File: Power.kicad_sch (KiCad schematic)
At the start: 51 parts, among them U1 STPMIC1APQR

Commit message: Layout started
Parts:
- added D1, D10, D11, D12, D13, D14, D2, D3, D4, D5, D6, D7, D8, D9: Red, SparkFun-LED:LED_0603_1608Metric, symbol SparkFun-LED:LED_Red_0603
- added R1, R10, R11, R14, R15, R16, R2, R3, R4, R5, R6, R7, R8, R9: 680, Resistor_SMD:R_0402_1005Metric, symbol SparkFun-Resistor:R
- renumbered R1 to R12, R2 to R13
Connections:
- net BSTOUT: now also D12.2 (A)
- net GND: now also R1.2, R10.2, R11.2, R14.2, R15.2, R16.2, R2.2, R3.2, R4.2, R5.2, R6.2, R7.2, R8.2, R9.2
- net LDO5OUT: now also D10.2 (A)
- net LDO6OUT: now also D11.2 (A)
- net VBUS_HOST: now also D14.2 (A)
- net VBUS_OTG: now also D13.2 (A)
- net VDD: now also D4.2 (A)
- net VDDA: now also D6.2 (A)
- net VDD_AUX: now also D5.2 (A)
- net VDD_CORE: now also D2.2 (A)
- net VDD_DDR: now also D3.2 (A)
- net VDD_NAND: now also D7.2 (A)
- net VDD_USB: now also D9.2 (A)
- net VIN: now also D1.2 (A)
- net VTT_DDR: now also D8.2 (A)
- new net: D8.1 (K), R8.1
- new net: D6.1 (K), R6.1
- new net: D2.1 (K), R2.1
- new net: D14.1 (K), R16.1
- new net: D3.1 (K), R3.1
- new net: D11.1 (K), R11.1
- new net: D10.1 (K), R10.1
- new net: D4.1 (K), R4.1
- new net: D7.1 (K), R7.1
- new net: D12.1 (K), R14.1
- new net: D5.1 (K), R5.1
- new net: D9.1 (K), R9.1
- new net: D1.1 (K), R1.1
- new net: D13.1 (K), R15.1
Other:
- moved on the sheet: CBUCK1IN1, CBUCK2IN1, CBUCK3IN1, CBUCK4IN1, CLDO16IN1, CLDO25IN1, CLDO3IN1, CVIN1, CVLXBST1, LXB1, NT1, NT2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

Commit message: Component placement
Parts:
- added H1, H2, H3, H4: MountingHole, MountingHole:MountingHole_3.2mm_M3, symbol Mechanical:MountingHole
- added TP22, TP23: RCWCTE, footprints:TP420X150, symbol RCWCTE:RCWCTE
- R12: footprint SparkFun-Resistor:R_0603_1608Metric -> Resistor_SMD:R_0402_1005Metric
- R13: footprint SparkFun-Resistor:R_0603_1608Metric -> LED_SMD:LED_0402_1005Metric
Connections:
- net GND: now also TP23.1
- net VIN: now also TP22.1

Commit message: Routed PMIC and started on MPU
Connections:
- net SWIN is gone; now on net BSTOUT: NT1.2, U1.37 (SWIN)
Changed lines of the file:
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@@
+	)
+	(junction
+		(at 250.19 83.82)
+		(diameter 0)
+		(color 0 0 0 0)
 	)
 	(junction
@@
 	(junction
 		(at 167.64 116.84)
+		(diameter 0)
+		(color 0 0 0 0)
+	)
+	(junction
+		(at 260.35 83.82)
 		(diameter 0)
 		(color 0 0 0 0)
@@
 	(wire
 		(pts
+			(xy 250.19 77.47) (xy 260.35 77.47)
+		)
+		(stroke
+			(width 0)
+			(type default)
+		)
+	)
+	(wire
+		(pts
 			(xy 22.86 44.45) (xy 35.56 44.45)
 		)
@@
 	(wire
 		(pts
+			(xy 260.35 77.47) (xy 260.35 83.82)
+		)
+		(stroke
+			(width 0)
+			(type default)
+		)
+	)
+	(wire
+		(pts
 			(xy 256.54 25.4) (xy 265.43 25.4)
 		)
@@
 	(wire
 		(pts
+			(xy 250.19 83.82) (xy 250.19 77.47)
+		)
+		(stroke
+			(width 0)
+			(type default)
+		)
+	)
+	(wire
+		(pts
 			(xy 193.04 120.65) (xy 193.04 116.84)
 		)
@@
 	(wire
 		(pts
-			(xy 257.81 83.82) (xy 267.97 83.82)
+			(xy 257.81 83.82) (xy 260.35 83.82)
 		)
 		(stroke
@@
 	(wire
 		(pts
-			(xy 242.57 83.82) (xy 252.73 83.82)
+			(xy 242.57 83.82) (xy 250.19 83.82)
 		)
 		(stroke
@@
 	(wire
 		(pts
+			(xy 250.19 83.82) (xy 252.73 83.82)
+		)
+		(stroke
+			(width 0)
+			(type default)
+		)
+	)
+	(wire
+		(pts
 			(xy 115.57 110.49) (xy 115.57 115.57)
 		)
@@
 		)
 		(stroke
+			(width 0)
+			(type default)
+		)
+	)
+	(wire
+		(pts
+			(xy 260.35 83.82) (xy 267.97 83.82)
+		)
+		(stroke

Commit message: Routing DDR
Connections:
- net VIN: no longer CLDO3IN1.1, NT3.2, U1.13 (LDO3IN)
- new net LDO3IN: CLDO3IN1.1, NT3.2, U1.13 (LDO3IN)
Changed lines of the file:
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@@
 	)
 	(junction
-		(at 256.54 25.4)
-		(diameter 0)
-		(color 0 0 0 0)
-	)
-	(junction
 		(at 104.14 181.61)
 		(diameter 0)
@@
 	(wire
 		(pts
-			(xy 256.54 22.86) (xy 256.54 25.4)
-		)
-		(stroke
-			(width 0)
-			(type default)
-		)
-	)
-	(wire
-		(pts
 			(xy 167.64 143.51) (xy 179.07 143.51)
 		)
@@
 					(unit 1)
 				)
-			)
-		)
-	)
-	(symbol
-		(lib_id "SparkFun-PowerSymbol:VIN")
-		(at 256.54 22.86 0)
-		(unit 1)
-		(exclude_from_sim no)
-		(in_bom yes)
-		(on_board yes)
-		(dnp no)
-		(fields_autoplaced yes)
-		(property "Reference" "#PWR08"
-			(at 256.54 26.67 0)
-			(effects
-				(font
-					(size 1.27 1.27)
-				)
-				(hide yes)
-			)
-		)
-		(property "Value" "VIN"
-			(at 256.54 19.05 0)
-			(do_not_autoplace yes)
-			(effects
-				(font
-					(size 1.27 1.27)
-				)
-			)
-		)
-		(property "Footprint" ""
-			(at 256.54 22.86 0)
-			(effects
-				(font
-					(size 1.27 1.27)
-				)
-				(hide yes)
-			)
-		)
-		(property "Datasheet" ""
-			(at 256.54 22.86 0)
-			(effects
-				(font
-					(size 1.27 1.27)
-				)
-				(hide yes)
-			)
-		)
-		(property "Description" "Power symbol creates a global label with name \"VIN\""
-			(at 256.54 22.86 0)
-			(effects
-				(font
-					(size 1.27 1.27)
-				)
-				(hide yes)
-			)
-		)
-		(pin "1"
-		)
-		(instances
-			(project "SBC"
-				(path "/21bb932a-ec67-4661-9215-0551f718d1c0/62ec818c-3f4b-42f5-b6cb-504a45fcd8bf"
-					(reference "#PWR08")
-					(unit 1)
-				)

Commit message: I am not good at routing
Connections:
- net BSTOUT: no longer NT1.2, U1.37 (SWIN)
- new net SWIN: NT1.2, U1.37 (SWIN)
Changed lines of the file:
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@@
 	(generator_version "8.0")
 	(paper "A4")
+	(bus_alias "BSTOUT"
+		(members "SWIN")
+	)
 	(junction
 		(at 95.25 181.61)
@@
 	)
 	(junction
-		(at 250.19 83.82)
-		(diameter 0)
-		(color 0 0 0 0)
-	)
-	(junction
 		(at 33.02 46.99)
 		(diameter 0)
@@
 	(junction
 		(at 167.64 116.84)
-		(diameter 0)
-		(color 0 0 0 0)
-	)
-	(junction
-		(at 260.35 83.82)
 		(diameter 0)
 		(color 0 0 0 0)
@@
 	(wire
 		(pts
-			(xy 250.19 77.47) (xy 260.35 77.47)
-		)
-		(stroke
-			(width 0)
-			(type default)
-		)
-	)
-	(wire
-		(pts
 			(xy 22.86 44.45) (xy 35.56 44.45)
 		)
@@
 	(wire
 		(pts
-			(xy 260.35 77.47) (xy 260.35 83.82)
-		)
-		(stroke
-			(width 0)
-			(type default)
-		)
-	)
-	(wire
-		(pts
 			(xy 256.54 25.4) (xy 265.43 25.4)
 		)
@@
 	(wire
 		(pts
-			(xy 250.19 83.82) (xy 250.19 77.47)
-		)
-		(stroke
-			(width 0)
-			(type default)
-		)
-	)
-	(wire
-		(pts
 			(xy 193.04 120.65) (xy 193.04 116.84)
 		)
@@
 	(wire
 		(pts
-			(xy 257.81 83.82) (xy 260.35 83.82)
+			(xy 257.81 83.82) (xy 267.97 83.82)
 		)
 		(stroke
@@
 	(wire
 		(pts
-			(xy 242.57 83.82) (xy 250.19 83.82)
+			(xy 242.57 83.82) (xy 252.73 83.82)
 		)
 		(stroke
@@
 	(wire
 		(pts
-			(xy 250.19 83.82) (xy 252.73 83.82)
-		)
-		(stroke
-			(width 0)
-			(type default)
-		)
-	)
-	(wire
-		(pts
 			(xy 115.57 110.49) (xy 115.57 115.57)
 		)
@@
 		)
 		(stroke
-			(width 0)
-			(type default)
-		)
-	)
-	(wire
-		(pts
-			(xy 260.35 83.82) (xy 267.97 83.82)
-		)
-		(stroke

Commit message: Everything is placed
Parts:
- removed NT1, NT2, NT3: NetTie_2, NetTie:NetTie-2_SMD_Pad0.5mm, symbol Device:NetTie_2
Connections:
- net LDO3IN is gone; now on net VDD_DDR: CLDO3IN1.1, U1.13 (LDO3IN)
- net SWIN is gone; now on net BSTOUT: U1.37 (SWIN)
- net VIO is gone; now on net VDD: R12.1, R13.1, U1.42 (VIO)
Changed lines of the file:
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@@
 	(generator_version "8.0")
 	(paper "A4")
-	(bus_alias "BSTOUT"
-		(members "SWIN")
-	)
 	(junction
 		(at 95.25 181.61)
@@
 	(wire
 		(pts
-			(xy 257.81 101.6) (xy 267.97 101.6)
-		)
-		(stroke
-			(width 0)
-			(type default)
-		)
-	)
-	(wire
-		(pts
 			(xy 33.02 46.99) (xy 35.56 46.99)
 		)
@@
 	(wire
 		(pts
-			(xy 257.81 92.71) (xy 267.97 92.71)
-		)
-		(stroke
-			(width 0)
-			(type default)
-		)
-	)
-	(wire
-		(pts
 			(xy 157.48 181.61) (xy 157.48 184.15)
 		)
@@
 	(wire
 		(pts
-			(xy 242.57 101.6) (xy 252.73 101.6)
+			(xy 242.57 101.6) (xy 267.97 101.6)
 		)
 		(stroke
@@
 	(wire
 		(pts
-			(xy 257.81 83.82) (xy 267.97 83.82)
-		)
-		(stroke
-			(width 0)
-			(type default)
-		)
-	)
-	(wire
-		(pts
 			(xy 22.86 52.07) (xy 35.56 52.07)
 		)
@@
 	(wire
 		(pts
-			(xy 242.57 83.82) (xy 252.73 83.82)
+			(xy 242.57 83.82) (xy 267.97 83.82)
 		)
 		(stroke
@@
 	(wire
 		(pts
-			(xy 242.57 92.71) (xy 252.73 92.71)
+			(xy 242.57 92.71) (xy 267.97 92.71)
 		)
 		(stroke
@@
 	)
 	(symbol
-		(lib_id "Device:NetTie_2")
-		(at 255.27 83.82 0)
-		(unit 1)
-		(exclude_from_sim no)
-		(in_bom no)
-		(on_board yes)
-		(dnp no)
-		(fields_autoplaced yes)
-		(property "Reference" "NT1"
-			(at 255.27 78.74 0)
-			(effects
-				(font
-					(size 1.27 1.27)
-				)
-			)
-		)
-		(property "Value" "NetTie_2"
-			(at 255.27 81.28 0)
-			(effects
-				(font
-					(size 1.27 1.27)
-				)
-			)
-		)
-		(property "Footprint" "NetTie:NetTie-2_SMD_Pad0.5mm"
-			(at 255.27 83.82 0)
-			(effects
-				(font
-					(size 1.27 1.27)
-				)
-				(hide yes)
-			)
-		)
-		(property "Datasheet" "~"
-			(at 255.27 83.82 0)
-			(effects
-				(font
-					(size 1.27 1.27)
-				)
-				(hide yes)
-			)
-		)
-		(property "Description" "Net tie, 2 pins"
-			(at 255.27 83.82 0)
-			(effects
-				(font
-					(size 1.27 1.27)
-				)
-				(hide yes)
-			)
-		)
-		(pin "2"
-		)
-		(pin "1"
-		)
-		(instances
-			(project ""
-				(path "/21bb932a-ec67-4661-9215-0551f718d1c0/62ec818c-3f4b-42f5-b6cb-504a45fcd8bf"
-					(reference "NT1")
-					(unit 1)
-				)
-			)
-		)
-	)
-	(symbol
 		(lib_id "SparkFun-Resistor:R")
 		(at 138.43 80.01 90)
@@
 	)
 	(symbol
-		(lib_id "Device:NetTie_2")
-		(at 255.27 92.71 0)
-		(unit 1)
-		(exclude_from_sim no)
-		(in_bom no)
-		(on_board yes)
-		(dnp no)
-		(fields_autoplaced yes)
-		(property "Reference" "NT2"
-			(at 255.27 87.63 0)
-			(effects
-				(font
-					(size 1.27 1.27)
-				)
-			)
-		)
-		(property "Value" "NetTie_2"
-			(at 255.27 90.17 0)
-			(effects
-				(font
-					(size 1.27 1.27)
-				)
-			)
-		)
-		(property "Footprint" "NetTie:NetTie-2_SMD_Pad0.5mm"
-			(at 255.27 92.71 0)
-			(effects
-				(font
-					(size 1.27 1.27)
-				)
-				(hide yes)
-			)
-		)
-		(property "Datasheet" "~"
-			(at 255.27 92.71 0)
-			(effects
-				(font
-					(size 1.27 1.27)
-				)
-				(hide yes)
-			)
-		)
-		(property "Description" "Net tie, 2 pins"
-			(at 255.27 92.71 0)
-			(effects
-				(font
-					(size 1.27 1.27)
-				)
-				(hide yes)
-			)
-		)
-		(pin "2"
-		)
-		(pin "1"
-		)
-		(instances
-			(project "SBC"
-				(path "/21bb932a-ec67-4661-9215-0551f718d1c0/62ec818c-3f4b-42f5-b6cb-504a45fcd8bf"
-					(reference "NT2")
-					(unit 1)
-				)
-			)
-		)
-	)
-	(symbol
 		(lib_id "power:GND")
 		(at 127 48.26 0)
@@
 					(unit 1)
 				)
-			)
-		)
-	)
-	(symbol
-		(lib_id "Device:NetTie_2")
-		(at 255.27 101.6 0)
-		(unit 1)
-		(exclude_from_sim no)
-		(in_bom no)
-		(on_board yes)
-		(dnp no)
-		(fields_autoplaced yes)
-		(property "Reference" "NT3"
-			(at 255.27 96.52 0)
-			(effects
-				(font
-					(size 1.27 1.27)
-				)
-			)
-		)
-		(property "Value" "NetTie_2"
-			(at 255.27 99.06 0)
-			(effects
-				(font
-					(size 1.27 1.27)
-				)
-			)
-		)
-		(property "Footprint" "NetTie:NetTie-2_SMD_Pad0.5mm"
-			(at 255.27 101.6 0)
-			(effects
-				(font
-					(size 1.27 1.27)
-				)
-				(hide yes)
-			)
-		)
-		(property "Datasheet" "~"
-			(at 255.27 101.6 0)
-			(effects
-				(font
-					(size 1.27 1.27)
-				)
-				(hide yes)
-			)
-		)
-		(property "Description" "Net tie, 2 pins"
-			(at 255.27 101.6 0)
-			(effects
-				(font
-					(size 1.27 1.27)
-				)
-				(hide yes)
-			)
-		)
-		(pin "2"
-		)
-		(pin "1"
-		)
-		(instances
-			(project "SBC"
-				(path "/21bb932a-ec67-4661-9215-0551f718d1c0/62ec818c-3f4b-42f5-b6cb-504a45fcd8bf"
-					(reference "NT3")
-					(unit 1)
-				)

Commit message: Started an entire reroute
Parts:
- D1, D10, D11, D12, D13, D14, D2, D3, D4, D5, D6, D7, D8, D9: footprint SparkFun-LED:LED_0603_1608Metric -> LED_SMD:LED_0603_1608Metric
- TP1, TP10, TP11, TP12, TP13, TP14, TP15, TP16, TP2, TP3, TP4, TP5, TP6, TP7, TP8, TP9: footprint SparkFun-Connector:TestPoint-0.5mm -> TestPoint:TestPoint_Pad_1.0x1.0mm

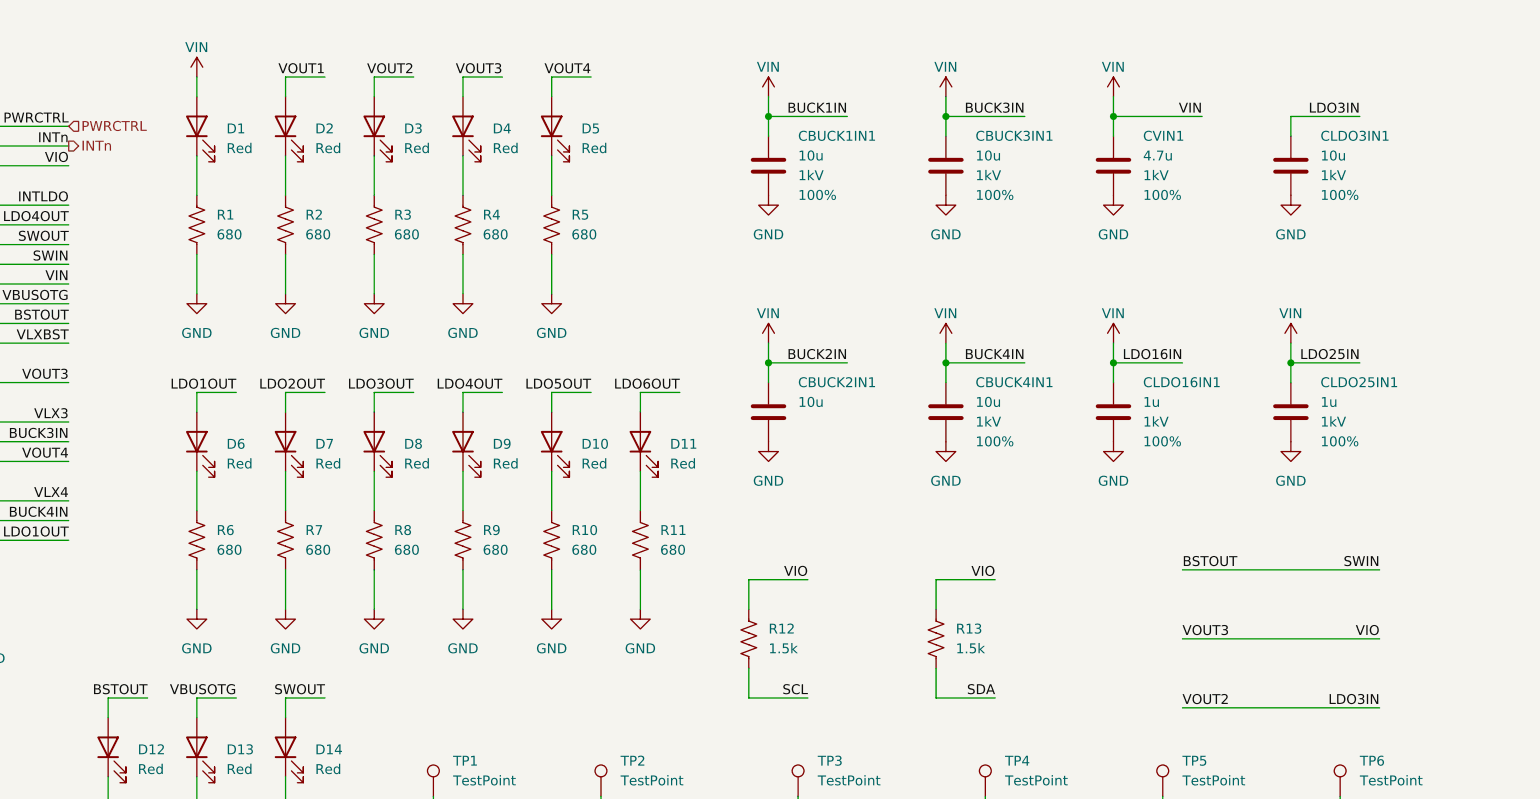
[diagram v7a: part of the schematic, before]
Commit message: PMIC Routing
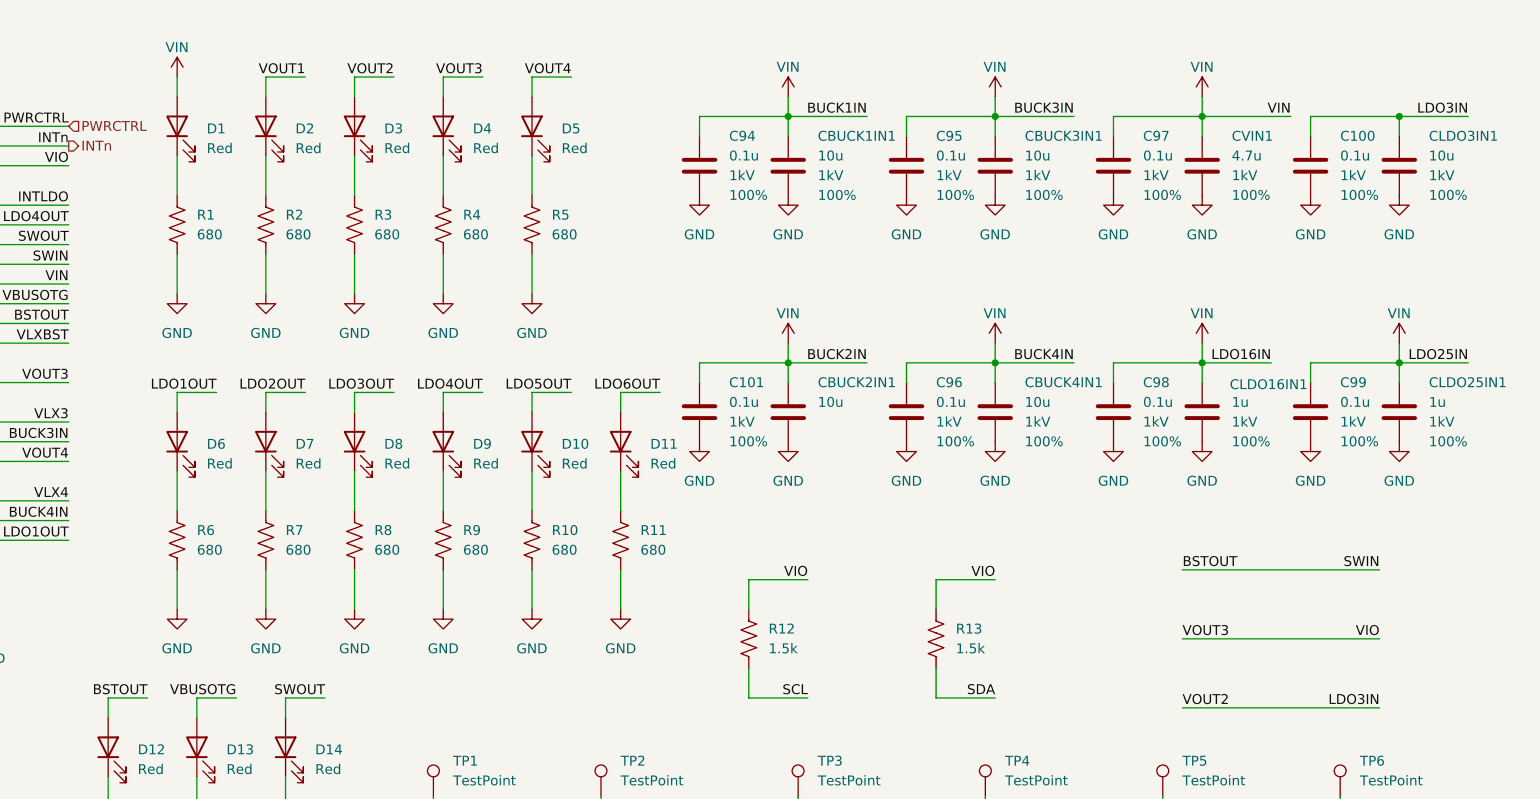
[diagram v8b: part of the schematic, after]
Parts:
- added C100, C101, C94, C95, C96, C97, C98, C99: 0.1u, Capacitor_SMD:C_0402_1005Metric, symbol SparkFun-Capacitor:C
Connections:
- net GND: now also C100.2, C101.2, C94.2, C95.2, C96.2, C97.2, C98.2, C99.2
- net VDD_DDR: now also C100.1
- net VIN: now also C101.1, C94.1, C95.1, C96.1, C97.1, C98.1, C99.1
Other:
- moved on the sheet: CBUCK1IN1, CBUCK2IN1, CBUCK3IN1, CBUCK4IN1, CLDO16IN1, CLDO25IN1, CLDO3IN1, CVIN1, D1, D10, D11, D2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
